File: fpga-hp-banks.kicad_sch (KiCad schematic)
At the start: 9 parts, among them U34 XCAU25P-2FFVB676I

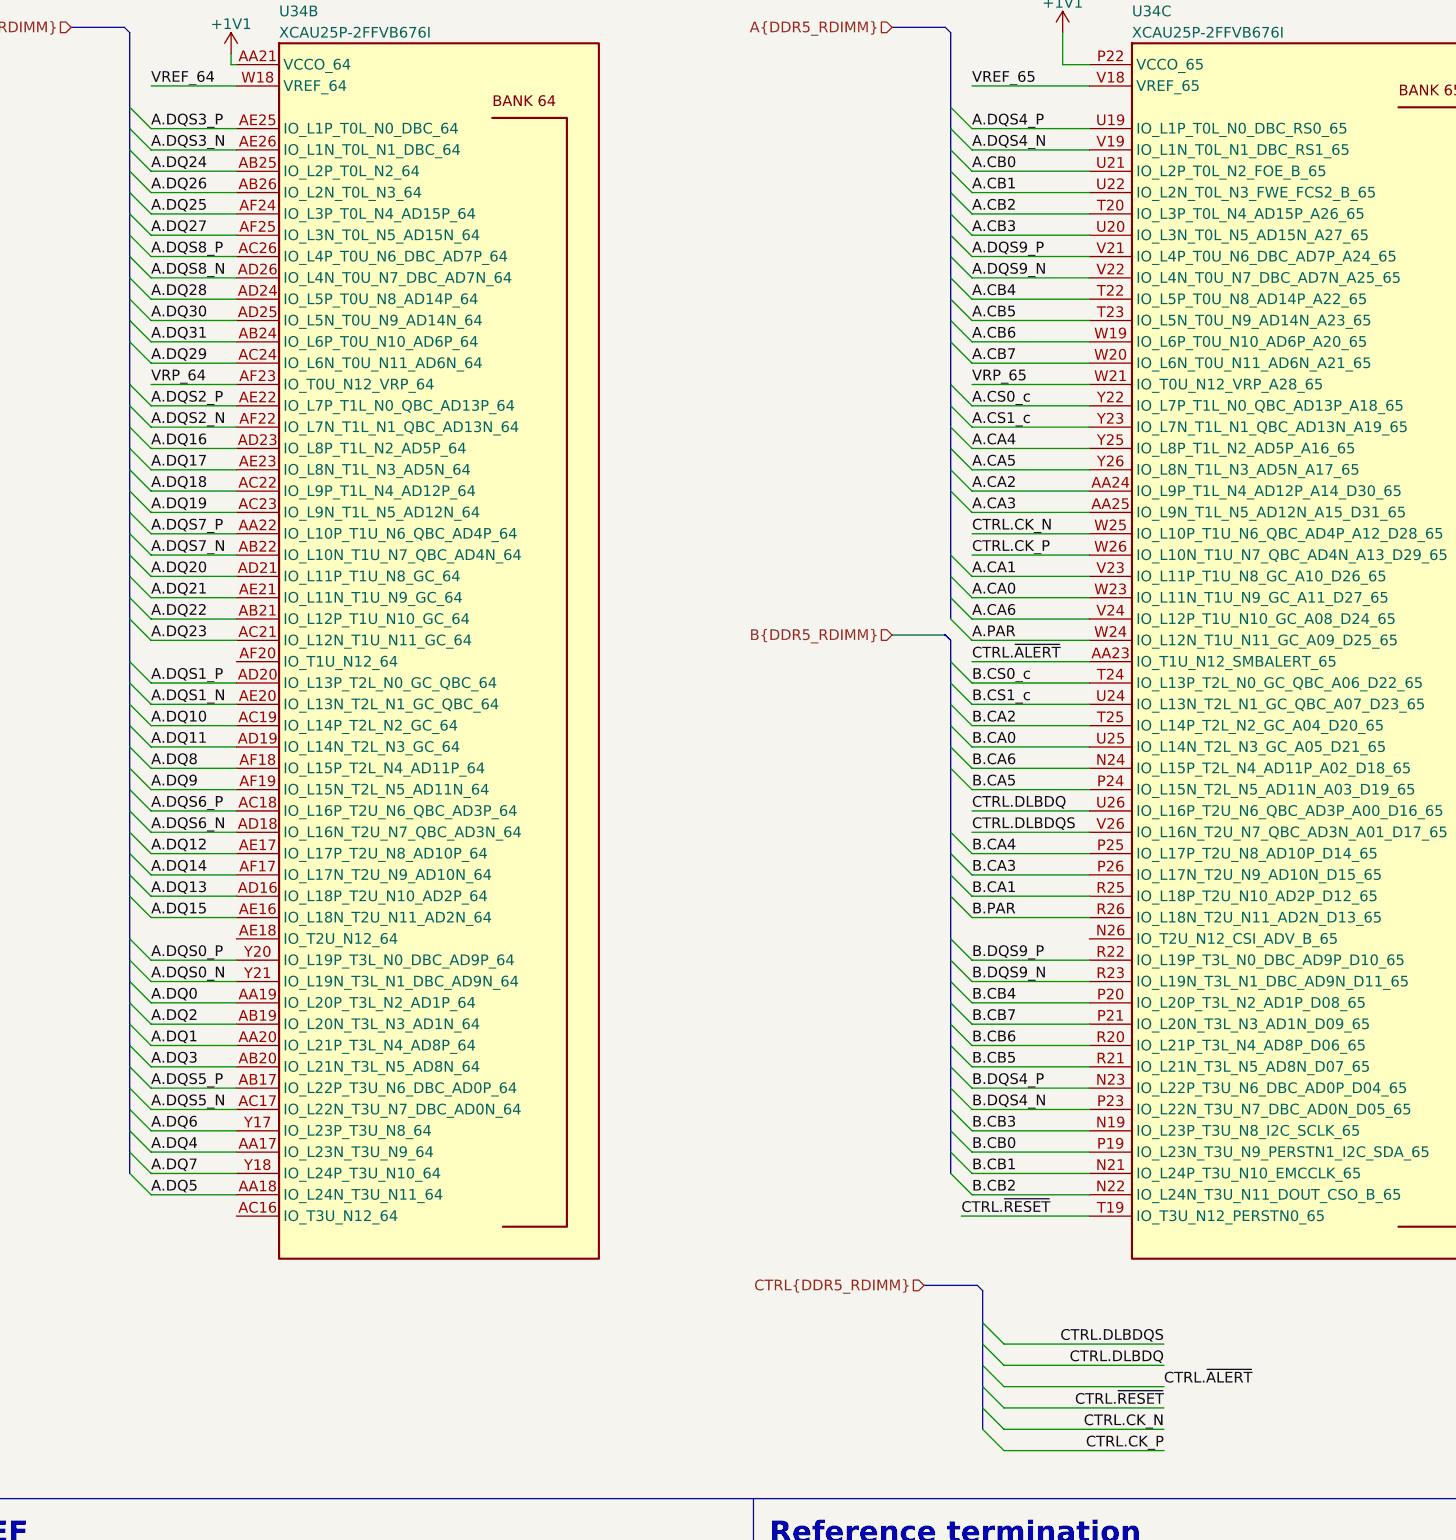
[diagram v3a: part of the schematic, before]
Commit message: [#66521] Optimize DDR5 RDIMM routing
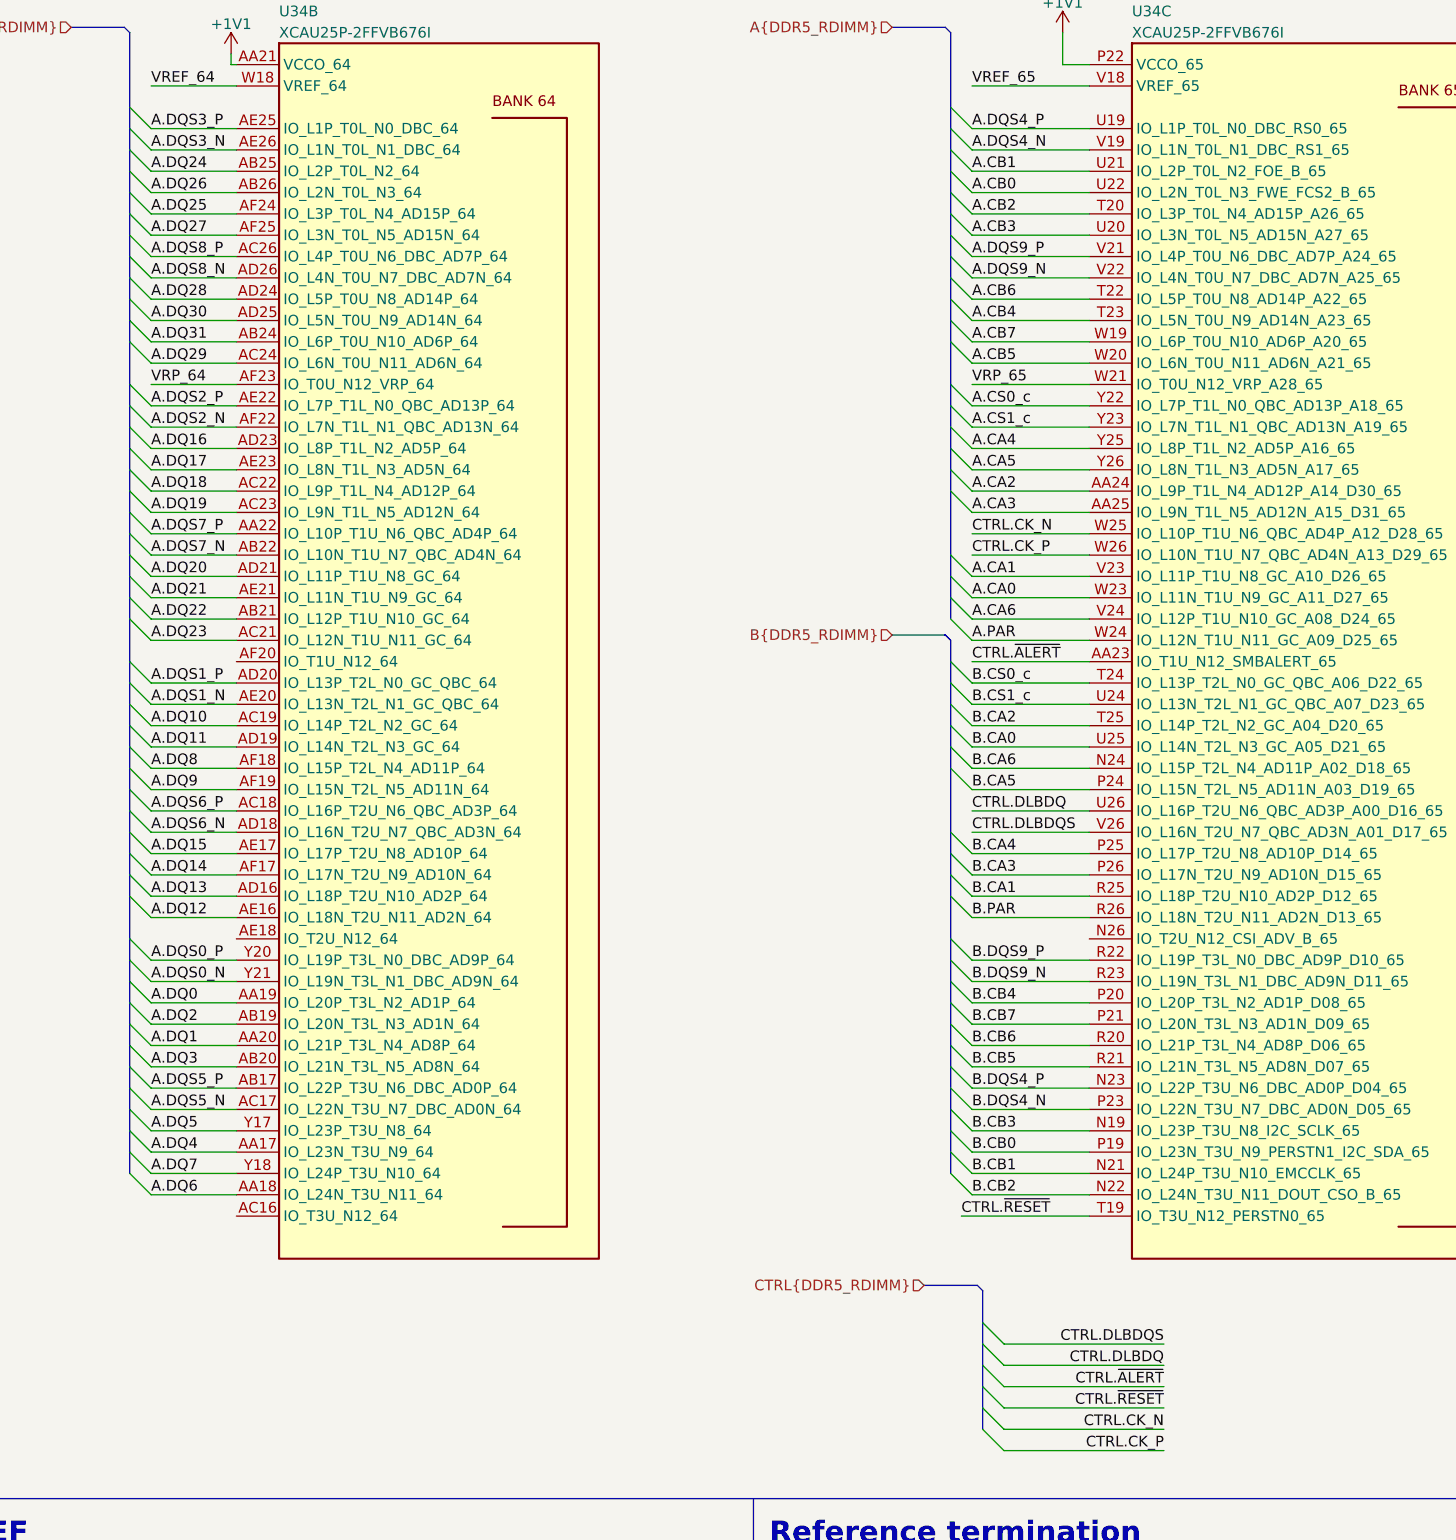
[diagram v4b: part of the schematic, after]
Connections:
- net A.CB0: now also U34.U22 (IO_L2N_T0L_N3_FWE_FCS2_B_65); no longer U34.U21 (IO_L2P_T0L_N2_FOE_B_65)
- net A.CB1: now also U34.U21 (IO_L2P_T0L_N2_FOE_B_65); no longer U34.U22 (IO_L2N_T0L_N3_FWE_FCS2_B_65)
- net A.CB4: now also U34.T23 (IO_L5N_T0U_N9_AD14N_A23_65); no longer U34.T22 (IO_L5P_T0U_N8_AD14P_A22_65)
- net A.CB5: now also U34.W20 (IO_L6N_T0U_N11_AD6N_A21_65); no longer U34.T23 (IO_L5N_T0U_N9_AD14N_A23_65)
- net A.CB6: now also U34.T22 (IO_L5P_T0U_N8_AD14P_A22_65); no longer U34.W19 (IO_L6P_T0U_N10_AD6P_A20_65)
- net A.CB7: now also U34.W19 (IO_L6P_T0U_N10_AD6P_A20_65); no longer U34.W20 (IO_L6N_T0U_N11_AD6N_A21_65)
- net A.DQ12: now also U34.AE16 (IO_L18N_T2U_N11_AD2N_64); no longer U34.AE17 (IO_L17P_T2U_N8_AD10P_64)
- net A.DQ15: now also U34.AE17 (IO_L17P_T2U_N8_AD10P_64); no longer U34.AE16 (IO_L18N_T2U_N11_AD2N_64)
- net A.DQ5: now also U34.Y17 (IO_L23P_T3U_N8_64); no longer U34.AA18 (IO_L24N_T3U_N11_64)
- net A.DQ6: now also U34.AA18 (IO_L24N_T3U_N11_64); no longer U34.Y17 (IO_L23P_T3U_N8_64)
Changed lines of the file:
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@@
     (effects (font (size 1.27 1.27)) (justify left bottom))
   )
-  (label "A.DQ5" (at 38.1 185.42 0) (fields_autoplaced)
+  (label "A.DQ5" (at 38.1 177.8 0) (fields_autoplaced)
     (effects (font (size 1.27 1.27)) (justify left bottom))
   )
@@
     (effects (font (size 1.27 1.27)) (justify left bottom))
   )
-  (label "CTRL.~{ALERT}" (at 158.75 208.28 0) (fields_autoplaced)
-    (effects (font (size 1.27 1.27)) (justify left bottom))
+  (label "CTRL.~{ALERT}" (at 158.75 208.28 180) (fields_autoplaced)
+    (effects (font (size 1.27 1.27)) (justify right bottom))
   )
   (label "B.DQ6" (at 245.11 86.36 0) (fields_autoplaced)
@@
     (effects (font (size 1.27 1.27)) (justify left bottom))
   )
-  (label "A.CB7" (at 135.89 86.36 0) (fields_autoplaced)
+  (label "A.CB7" (at 135.89 83.82 0) (fields_autoplaced)
     (effects (font (size 1.27 1.27)) (justify left bottom))
   )
@@
     (effects (font (size 1.27 1.27)) (justify left bottom))
   )
-  (label "A.DQ6" (at 38.1 177.8 0) (fields_autoplaced)
+  (label "A.DQ6" (at 38.1 185.42 0) (fields_autoplaced)
     (effects (font (size 1.27 1.27)) (justify left bottom))
   )
@@
     (effects (font (size 1.27 1.27)) (justify left bottom))
   )
-  (label "A.CB1" (at 135.89 66.04 0) (fields_autoplaced)
+  (label "A.CB1" (at 135.89 63.5 0) (fields_autoplaced)
     (effects (font (size 1.27 1.27)) (justify left bottom))
   )
@@
     (effects (font (size 1.27 1.27)) (justify left bottom))
   )
-  (label "A.CB4" (at 135.89 78.74 0) (fields_autoplaced)
+  (label "A.CB4" (at 135.89 81.28 0) (fields_autoplaced)
     (effects (font (size 1.27 1.27)) (justify left bottom))
   )
@@
     (effects (font (size 1.27 1.27)) (justify left bottom))
   )
-  (label "A.DQ15" (at 38.1 152.4 0) (fields_autoplaced)
+  (label "A.DQ15" (at 38.1 144.78 0) (fields_autoplaced)
     (effects (font (size 1.27 1.27)) (justify left bottom))
   )
@@
     (effects (font (size 1.27 1.27)) (justify left bottom))
   )
-  (label "A.DQ12" (at 38.1 144.78 0) (fields_autoplaced)
+  (label "A.DQ12" (at 38.1 152.4 0) (fields_autoplaced)
     (effects (font (size 1.27 1.27)) (justify left bottom))
   )
@@
     (effects (font (size 1.27 1.27)) (justify left bottom))
   )
-  (label "A.CB0" (at 135.89 63.5 0) (fields_autoplaced)
+  (label "A.CB0" (at 135.89 66.04 0) (fields_autoplaced)
     (effects (font (size 1.27 1.27)) (justify left bottom))
   )
@@
     (effects (font (size 1.27 1.27)) (justify left bottom))
   )
-  (label "A.CB5" (at 135.89 81.28 0) (fields_autoplaced)
+  (label "A.CB5" (at 135.89 86.36 0) (fields_autoplaced)
     (effects (font (size 1.27 1.27)) (justify left bottom))
   )
@@
     (effects (font (size 1.27 1.27)) (justify left bottom))
   )
-  (label "A.CB6" (at 135.89 83.82 0) (fields_autoplaced)
-    (effects (font (size 1.27 1.27)) (justify left bottom))
-  )
+  (label "A.CB6" (at 135.89 78.74 0) (fields_autoplaced)
+    (effects (font (size 1.27 1.27)) (justify left bottom))
+  )

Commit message: [#67016] Add RGMII, Hyper Ram and SD card schematic connection
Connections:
- net SD.DAT2: now reaches U34.D18 (IO_L11N_T1U_N9_GC_67)
- net SD.DAT3: now reaches U34.D19 (IO_L12P_T1U_N10_GC_67)
- net SD.CD: now reaches U34.D20 (IO_L12N_T1U_N11_GC_67)
- net SD.DAT1: now reaches U34.E18 (IO_L11P_T1U_N8_GC_67)
- net SD.DAT0: now reaches U34.E20 (IO_L10N_T1U_N7_QBC_AD4N_67)
- net SD.CLK: now reaches U34.F20 (IO_L10P_T1U_N6_QBC_AD4P_67)
- net SD.CMD: now reaches U34.G21 (IO_L9N_T1L_N5_AD12N_67)
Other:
- note added: "Pinout 1.1.1"
- note removed: "Pinout 1.1.0"
- moved on the sheet: U34C, U34D, U34E

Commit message: [#67016] Add ETH layout
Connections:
- net ETH.MDC: now also U34.C21 (IO_L22P_T3U_N6_DBC_AD0P_67); no longer U34.A18 (IO_L16N_T2U_N7_QBC_AD3N_67)
- net ETH.MDIO: now also U34.D21 (IO_L20N_T3L_N3_AD1N_67); no longer U34.A17 (IO_L16P_T2U_N6_QBC_AD3P_67)
- net ETH.REF_CLK: now also U34.E21 (IO_L20P_T3L_N2_AD1P_67); no longer U34.D21 (IO_L20N_T3L_N3_AD1N_67)
- net ETH.RXC: now also U34.A19 (IO_L18P_T2U_N10_AD2P_67); no longer U34.B15 (IO_L17P_T2U_N8_AD10P_67)
- net ETH.RXD0: now also U34.A18 (IO_L16N_T2U_N7_QBC_AD3N_67); no longer U34.B17 (IO_L15N_T2L_N5_AD11N_67)
- net ETH.RXD1: now also U34.B17 (IO_L15N_T2L_N5_AD11N_67); no longer U34.C17 (IO_L15P_T2L_N4_AD11P_67)
- net ETH.RXD2: now also U34.B16 (IO_T2U_N12_67); no longer U34.B20 (IO_L14N_T2L_N3_GC_67)
- net ETH.RXD3: now also U34.B15 (IO_L17P_T2U_N8_AD10P_67); no longer U34.B19 (IO_L14P_T2L_N2_GC_67)
- net ETH.RX_CTL: now also U34.A20 (IO_L18N_T2U_N11_AD2N_67); no longer U34.E21 (IO_L20P_T3L_N2_AD1P_67)
- net ETH.TXC: now also U34.A22 (IO_L19P_T3L_N0_DBC_AD9P_67); no longer U34.A15 (IO_L17N_T2U_N9_AD10N_67)
- net ETH.TXD0: now also U34.A17 (IO_L16P_T2U_N6_QBC_AD3P_67); no longer U34.A19 (IO_L18P_T2U_N10_AD2P_67)
- net ETH.TXD1: now also U34.B19 (IO_L14P_T2L_N2_GC_67); no longer U34.A20 (IO_L18N_T2U_N11_AD2N_67)
- net ETH.TXD2: now also U34.B20 (IO_L14N_T2L_N3_GC_67); no longer U34.B16 (IO_T2U_N12_67)
- net ETH.TXD3: now also U34.C17 (IO_L15P_T2L_N4_AD11P_67); no longer U34.A22 (IO_L19P_T3L_N0_DBC_AD9P_67)
- net ETH.TX_CTL: now also U34.A15 (IO_L17N_T2U_N9_AD10N_67); no longer U34.C21 (IO_L22P_T3U_N6_DBC_AD0P_67)
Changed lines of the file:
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@@
     (effects (font (size 1.27 1.27)) (justify left bottom))
   )
-  (label "ETH.RXC" (at 313.69 144.78 0) (fields_autoplaced)
+  (label "ETH.RXC" (at 313.69 149.86 0) (fields_autoplaced)
     (effects (font (size 1.27 1.27)) (justify left bottom))
   )
@@
     (effects (font (size 1.27 1.27)) (justify left bottom))
   )
-  (label "ETH.TXD0" (at 313.69 149.86 0) (fields_autoplaced)
+  (label "ETH.TXD0" (at 313.69 139.7 0) (fields_autoplaced)
     (effects (font (size 1.27 1.27)) (justify left bottom))
   )
@@
     (effects (font (size 1.27 1.27)) (justify right bottom))
   )
-  (label "ETH.RX_CTL" (at 313.69 162.56 0) (fields_autoplaced)
+  (label "ETH.RX_CTL" (at 313.69 152.4 0) (fields_autoplaced)
     (effects (font (size 1.27 1.27)) (justify left bottom))
   )
@@
     (effects (font (size 1.27 1.27)) (justify left bottom))
   )
-  (label "ETH.REF_CLK" (at 313.69 165.1 0) (fields_autoplaced)
+  (label "ETH.REF_CLK" (at 313.69 162.56 0) (fields_autoplaced)
     (effects (font (size 1.27 1.27)) (justify left bottom))
   )
@@
     (effects (font (size 1.27 1.27)) (justify left bottom))
   )
-  (label "ETH.TX_CTL" (at 313.69 172.72 0) (fields_autoplaced)
+  (label "ETH.TX_CTL" (at 313.69 147.32 0) (fields_autoplaced)
     (effects (font (size 1.27 1.27)) (justify left bottom))
   )
@@
     (effects (font (size 1.27 1.27)) (justify left bottom))
   )
-  (label "ETH.RXD1" (at 313.69 134.62 0) (fields_autoplaced)
+  (label "ETH.RXD1" (at 313.69 137.16 0) (fields_autoplaced)
     (effects (font (size 1.27 1.27)) (justify left bottom))
   )
@@
     (effects (font (size 1.27 1.27)) (justify left bottom))
   )
-  (label "ETH.TXD3" (at 313.69 157.48 0) (fields_autoplaced)
+  (label "ETH.TXD3" (at 313.69 134.62 0) (fields_autoplaced)
     (effects (font (size 1.27 1.27)) (justify left bottom))
   )
@@
     (effects (font (size 1.27 1.27)) (justify left bottom))
   )
-  (label "ETH.MDC" (at 313.69 142.24 0) (fields_autoplaced)
+  (label "ETH.MDC" (at 313.69 172.72 0) (fields_autoplaced)
     (effects (font (size 1.27 1.27)) (justify left bottom))
   )
@@
     (effects (font (size 1.27 1.27)) (justify left bottom))
   )
-  (label "ETH.TXD2" (at 313.69 154.94 0) (fields_autoplaced)
+  (label "ETH.TXD2" (at 313.69 132.08 0) (fields_autoplaced)
     (effects (font (size 1.27 1.27)) (justify left bottom))
   )
@@
     (effects (font (size 1.27 1.27)) (justify left bottom))
   )
-  (label "ETH.RXD2" (at 313.69 132.08 0) (fields_autoplaced)
+  (label "ETH.RXD2" (at 313.69 154.94 0) (fields_autoplaced)
     (effects (font (size 1.27 1.27)) (justify left bottom))
   )
@@
     (effects (font (size 1.27 1.27)) (justify left bottom))
   )
-  (label "ETH.RXD0" (at 313.69 137.16 0) (fields_autoplaced)
+  (label "ETH.RXD0" (at 313.69 142.24 0) (fields_autoplaced)
     (effects (font (size 1.27 1.27)) (justify left bottom))
   )
@@
     (effects (font (size 1.27 1.27)) (justify left bottom))
   )
-  (label "ETH.TXD1" (at 313.69 152.4 0) (fields_autoplaced)
+  (label "ETH.TXD1" (at 313.69 129.54 0) (fields_autoplaced)
     (effects (font (size 1.27 1.27)) (justify left bottom))
   )
@@
     (effects (font (size 1.27 1.27)) (justify left bottom))
   )
-  (label "ETH.RXD3" (at 313.69 129.54 0) (fields_autoplaced)
+  (label "ETH.RXD3" (at 313.69 144.78 0) (fields_autoplaced)
     (effects (font (size 1.27 1.27)) (justify left bottom))
   )
@@
     (effects (font (size 1.27 1.27)) (justify left bottom))
   )
-  (label "ETH.TXC" (at 313.69 147.32 0) (fields_autoplaced)
+  (label "ETH.TXC" (at 313.69 157.48 0) (fields_autoplaced)
     (effects (font (size 1.27 1.27)) (justify left bottom))
   )
@@
     (effects (font (size 1.27 1.27)) (justify left bottom))
   )
-  (label "ETH.MDIO" (at 313.69 139.7 0) (fields_autoplaced)
-    (effects (font (size 1.27 1.27)) (justify left bottom))
-  )
+  (label "ETH.MDIO" (at 313.69 165.1 0) (fields_autoplaced)
+    (effects (font (size 1.27 1.27)) (justify left bottom))
+  )
